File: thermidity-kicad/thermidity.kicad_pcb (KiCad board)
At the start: 2 copper layers, 60 x 30 mm, 17 parts, among them J1 Battery, J2 Display, J3 ISP, U1 ATmega328P, U2 HIH-5030, U3 TMP36

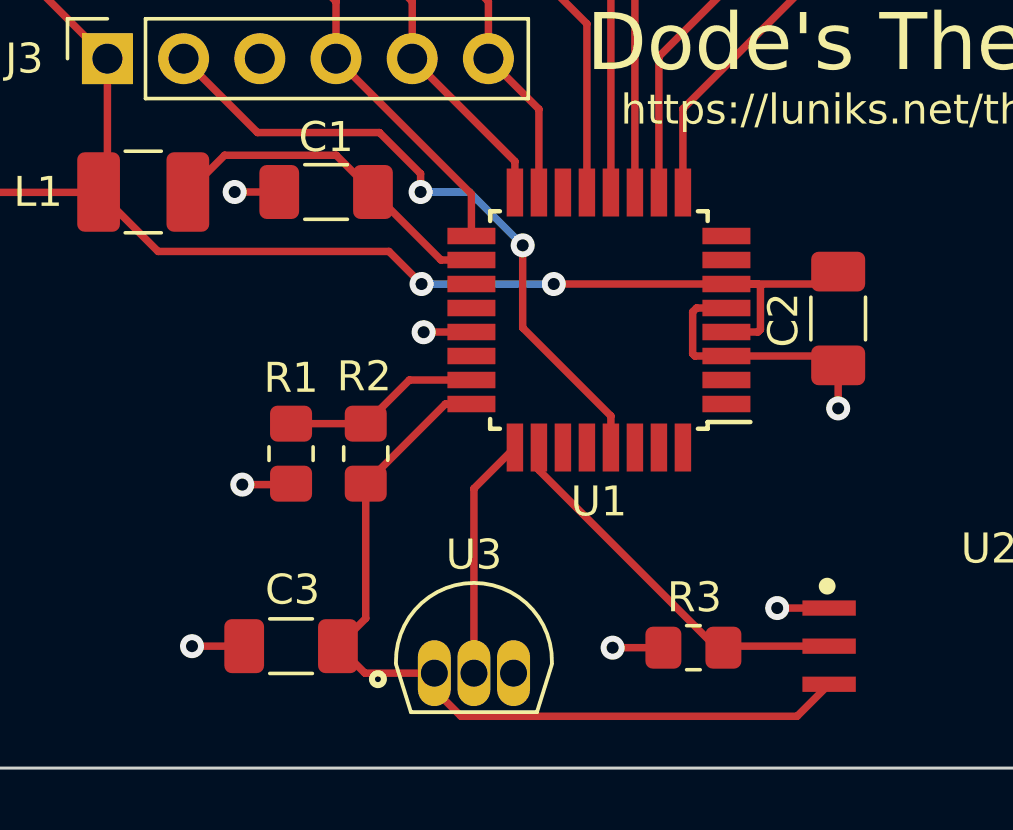
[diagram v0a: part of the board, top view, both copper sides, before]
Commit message: ratiometric measurement of temperature
- replace TMP36 with a thermistor NTC 100k
- put back 1nF cap between AREF and GND
- wait 150us for the cap to discharge before converting with 1.1V reference
- uint16_t is enough for 16x ADC
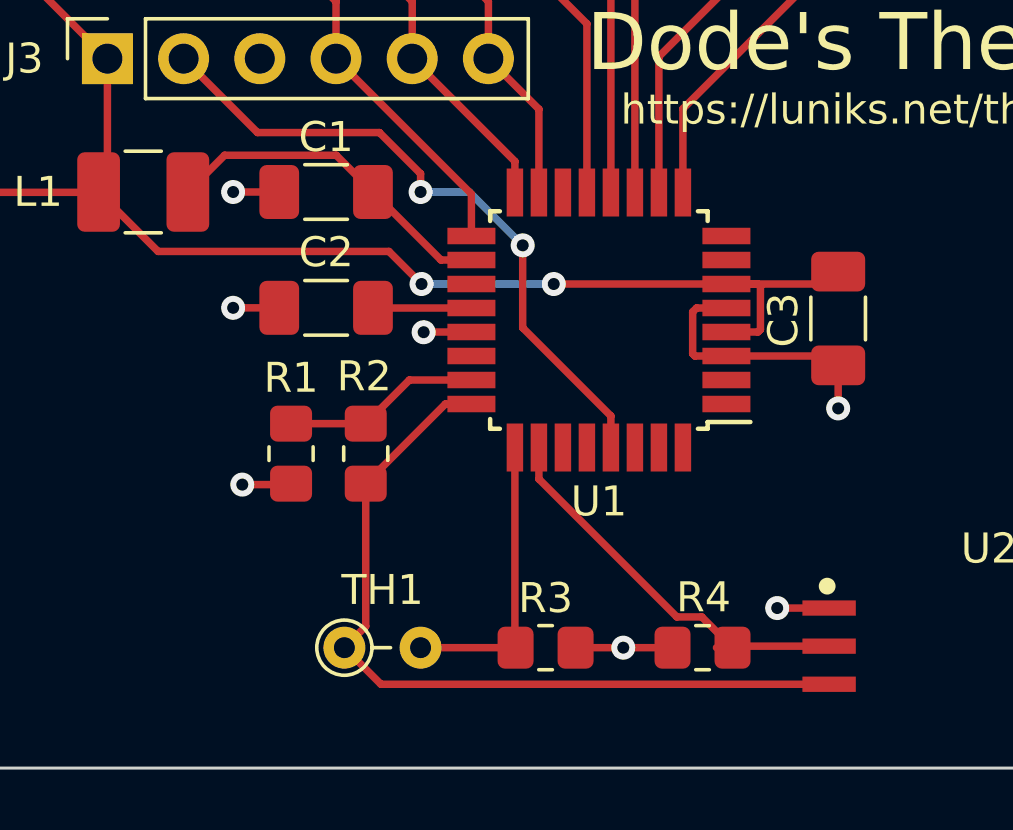
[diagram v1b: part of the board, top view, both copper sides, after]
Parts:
- removed the C3 at (135.2, 84.8)
- removed U3: TMP36, TMP36GT9:XDCR_TMP36GT9
- added C2: 1nF, Capacitor_SMD:C_1206_3216Metric_Pad1.33x1.80mm_HandSolder, F.Cu at (136.3, 73.6)
- added R3: 100k, Resistor_SMD:R_0805_2012Metric_Pad1.20x1.40mm_HandSolder, F.Cu at (143.7, 84.9)
- added TH1: NTC 100k, Resistor_THT:R_Axial_DIN0204_L3.6mm_D1.6mm_P2.54mm_Vertical, F.Cu at (137.0, 84.9)
- R1: value 1M -> 300K
- R2: value 1M -> 1.2M
- moved R4 0.30 mm to (148.9, 84.9)
- renumbered C2 to C3, R3 to R4
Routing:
- net unconnected-(U1-Pad20): track 0.00 -> 3.28 mm
- net Net-(U1-Pad25): track 8.09 -> 9.85 mm
- net Net-(R2-Pad1): track 28.5 -> 27.0 mm
- net GND: track 19.2 -> 20.5 mm
- net Net-(R4-Pad1): track 13.0 -> 13.7 mm

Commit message: ratiometric measurement of temperature
- SMD footprint instead of TH for thermistor
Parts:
- TH1: footprint Resistor_THT:R_Axial_DIN0204_L3.6mm_D1.6mm_P2.54mm_Vertical -> Resistor_SMD:R_1206_3216Metric_Pad1.30x1.75mm_HandSolder
- moved TH1 1.27 mm to (138.2, 84.9)
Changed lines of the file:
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@@
     )
   )
-  (footprint "Resistor_THT:R_Axial_DIN0204_L3.6mm_D1.6mm_P2.54mm_Vertical" (layer "F.Cu")
-    (at 136.956 84.8868)
-    (descr "Resistor, Axial_DIN0204 series, Axial, Vertical, pin pitch=2.54mm, 0.167W, length*diameter=3.6*1.6mm^2, http://cdn-reichelt.de/documents/datenblatt/B400/1_4W%23YAG.pdf")
-    (tags "Resistor Axial_DIN0204 series Axial Vertical pin pitch 2.54mm 0.167W length 3.6mm diameter 1.6mm")
-    (property "Sheetfile" "thermidity.kicad_sch")
-    (property "Sheetname" "")
-    (attr through_hole)
-    (fp_text reference "TH1" (at 1.27 -1.92) (layer "F.SilkS")
-      (effects (font (size 1 1) (thickness 0.15)))
-    )
-    (fp_text value "NTC 100k" (at 1.27 1.92) (layer "F.Fab")
-      (effects (font (size 1 1) (thickness 0.15)))
-    )
-    (fp_text user "${REFERENCE}" (at 1.27 -1.92) (layer "F.Fab")
-      (effects (font (size 1 1) (thickness 0.15)))
-    )
-    (fp_line (start 0.92 0) (end 1.54 0) (layer "F.SilkS") (width 0.12))
-    (fp_circle (center 0 0) (end 0.92 0) (layer "F.SilkS") (width 0.12) (fill none))
-    (fp_line (start 3.49 1.05) (end 3.49 -1.05) (layer "F.CrtYd") (width 0.05))
-    (fp_line (start 3.49 -1.05) (end -1.05 -1.05) (layer "F.CrtYd") (width 0.05))
-    (fp_line (start -1.05 1.05) (end 3.49 1.05) (layer "F.CrtYd") (width 0.05))
-    (fp_line (start -1.05 -1.05) (end -1.05 1.05) (layer "F.CrtYd") (width 0.05))
-    (fp_line (start 0 0) (end 2.54 0) (layer "F.Fab") (width 0.1))
-    (fp_circle (center 0 0) (end 0.8 0) (layer "F.Fab") (width 0.1) (fill none))
-    (pad "1" thru_hole circle (at 0 0) (size 1.4 1.4) (drill 0.7) (layers *.Cu *.Mask)
+  (footprint "Resistor_SMD:R_1206_3216Metric_Pad1.30x1.75mm_HandSolder" (layer "F.Cu")
+    (at 138.2268 84.8868)
+    (descr "Resistor SMD 1206 (3216 Metric), square (rectangular) end terminal, IPC_7351 nominal with elongated pad for handsoldering. (Body size source: IPC-SM-782 page 72, https://www.pcb-3d.com/wordpress/wp-content/uploads/ipc-sm-782a_amendment_1_and_2.pdf), generated with kicad-footprint-generator")
+    (tags "resistor handsolder")
+    (property "Sheetfile" "thermidity.kicad_sch")
+    (property "Sheetname" "")
+    (attr smd)
+    (fp_text reference "TH1" (at 0 -1.82) (layer "F.SilkS")
+      (effects (font (size 1 1) (thickness 0.15)))
+    )
+    (fp_text value "NTC 100k" (at 0 1.82) (layer "F.Fab")
+      (effects (font (size 1 1) (thickness 0.15)))
+    )
+    (fp_text user "${REFERENCE}" (at 0 0) (layer "F.Fab")
+      (effects (font (size 0.8 0.8) (thickness 0.12)))
+    )
+    (fp_line (start -0.727064 0.91) (end 0.727064 0.91) (layer "F.SilkS") (width 0.12))
+    (fp_line (start -0.727064 -0.91) (end 0.727064 -0.91) (layer "F.SilkS") (width 0.12))
+    (fp_line (start 2.45 1.12) (end -2.45 1.12) (layer "F.CrtYd") (width 0.05))
+    (fp_line (start -2.45 -1.12) (end 2.45 -1.12) (layer "F.CrtYd") (width 0.05))
+    (fp_line (start -2.45 1.12) (end -2.45 -1.12) (layer "F.CrtYd") (width 0.05))
+    (fp_line (start 2.45 -1.12) (end 2.45 1.12) (layer "F.CrtYd") (width 0.05))
+    (fp_line (start -1.6 0.8) (end -1.6 -0.8) (layer "F.Fab") (width 0.1))
+    (fp_line (start -1.6 -0.8) (end 1.6 -0.8) (layer "F.Fab") (width 0.1))
+    (fp_line (start 1.6 0.8) (end -1.6 0.8) (layer "F.Fab") (width 0.1))
+    (fp_line (start 1.6 -0.8) (end 1.6 0.8) (layer "F.Fab") (width 0.1))
+    (pad "1" smd roundrect (at -1.55 0) (size 1.3 1.75) (layers "F.Cu" "F.Paste" "F.Mask") (roundrect_rratio 0.192308)
       (net 15 "Net-(R2-Pad1)") (pintype "passive"))
-    (pad "2" thru_hole oval (at 2.54 0) (size 1.4 1.4) (drill 0.7) (layers *.Cu *.Mask)
+    (pad "2" smd roundrect (at 1.55 0) (size 1.3 1.75) (layers "F.Cu" "F.Paste" "F.Mask") (roundrect_rratio 0.192308)
       (net 24 "Net-(U1-Pad25)") (pintype "passive"))
-    (model "${KICAD6_3DMODEL_DIR}/Resistor_THT.3dshapes/R_Axial_DIN0204_L3.6mm_D1.6mm_P2.54mm_Vertical.wrl"
+    (model "${KICAD6_3DMODEL_DIR}/Resistor_SMD.3dshapes/R_1206_3216Metric.wrl"
       (offset (xyz 0 0 0))
       (scale (xyz 1 1 1))
@@
   (segment (start 141.1224 69.6976) (end 142.9004 71.4756) (width 0.25) (layer "B.Cu") (net 14))
   (segment (start 139.4968 69.6976) (end 141.1224 69.6976) (width 0.25) (layer "B.Cu") (net 14))
-  (segment (start 138.1752 86.106) (end 153.1142 86.106) (width 0.25) (layer "F.Cu") (net 15))
   (segment (start 140.3224 76.7648) (end 137.668 79.4192) (width 0.25) (layer "F.Cu") (net 15))
-  (segment (start 137.668 84.1748) (end 136.956 84.8868) (width 0.25) (layer "F.Cu") (net 15))
-  (segment (start 137.668 79.4192) (end 137.668 84.1748) (width 0.25) (layer "F.Cu") (net 15))
-  (segment (start 136.956 84.8868) (end 138.1752 86.106) (width 0.25) (layer "F.Cu") (net 15))
+  (segment (start 136.6768 84.8868) (end 137.896 86.106) (width 0.25) (layer "F.Cu") (net 15))
+  (segment (start 137.896 86.106) (end 153.1142 86.106) (width 0.25) (layer "F.Cu") (net 15))
+  (segment (start 137.668 83.8956) (end 136.6768 84.8868) (width 0.25) (layer "F.Cu") (net 15))
+  (segment (start 137.668 79.4192) (end 137.668 83.8956) (width 0.25) (layer "F.Cu") (net 15))
   (segment (start 141.1904 76.7648) (end 140.3224 76.7648) (width 0.25) (layer "F.Cu") (net 15))
   (segment (start 137.9161 73.5648) (end 137.9097 73.5584) (width 0.25) (layer "F.Cu") (net 16))
   (segment (start 141.1904 73.5648) (end 137.9161 73.5648) (width 0.25) (layer "F.Cu") (net 16))
-  (segment (start 139.496 84.8868) (end 142.6624 84.8868) (width 0.25) (layer "F.Cu") (net 24))
+  (segment (start 142.6624 84.8868) (end 139.7768 84.8868) (width 0.25) (layer "F.Cu") (net 24))
   (segment (start 142.6404 78.2148) (end 142.6404 84.8648) (width 0.25) (layer "F.Cu") (net 24))
   (segment (start 142.6404 84.8648) (end 142.6624 84.8868) (width 0.25) (layer "F.Cu") (net 24))

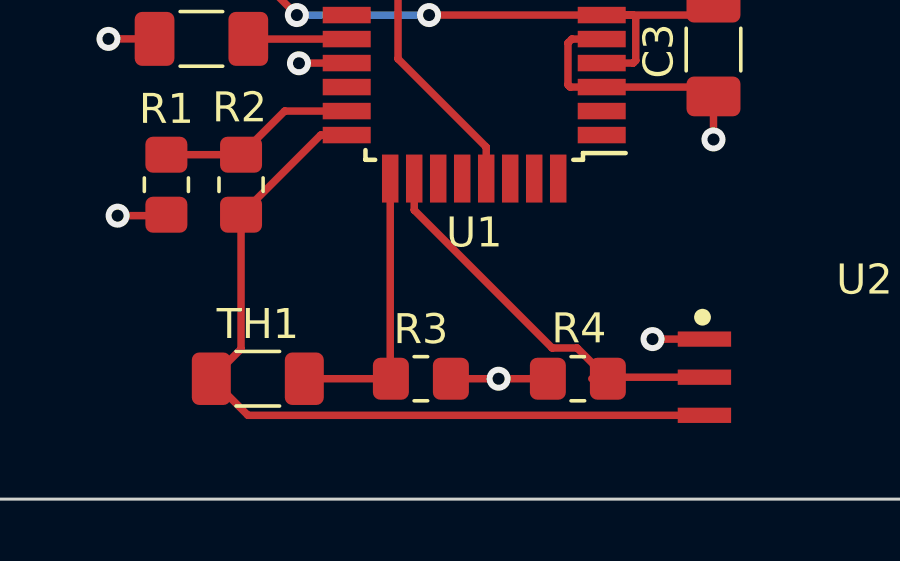
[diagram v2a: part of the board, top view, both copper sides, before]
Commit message: ratiometric measurement of temperature
- calculate temperature
- rounding of temperature compensated relative humidity
- no need for battery voltage in mV
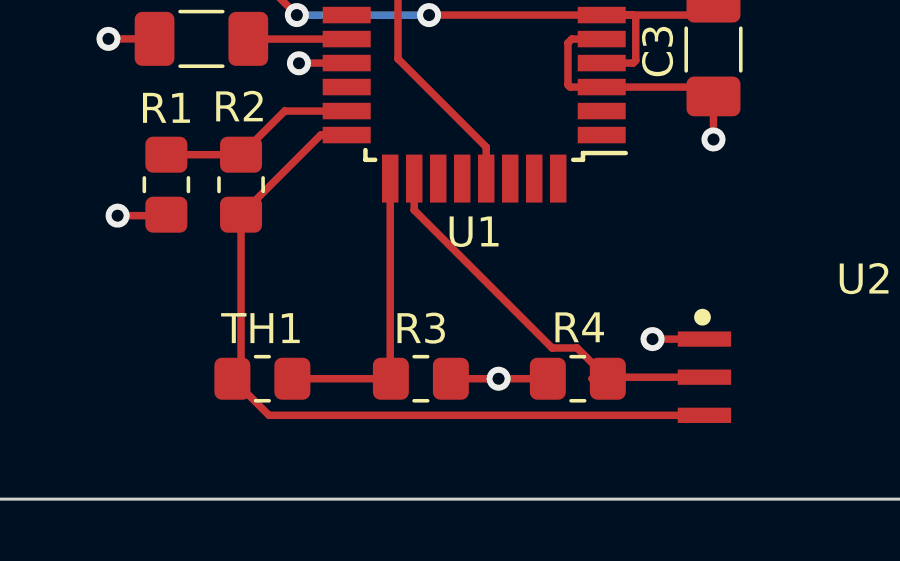
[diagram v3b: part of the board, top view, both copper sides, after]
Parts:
- TH1: footprint Resistor_SMD:R_1206_3216Metric_Pad1.30x1.75mm_HandSolder -> Resistor_SMD:R_0805_2012Metric_Pad1.20x1.40mm_HandSolder
- moved TH1 0.15 mm to (138.4, 84.9)
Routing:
- net Net-(R2-Pad1): track 27.4 -> 26.4 mm
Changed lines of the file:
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@@
     )
   )
-  (footprint "Resistor_SMD:R_1206_3216Metric_Pad1.30x1.75mm_HandSolder" (layer "F.Cu")
-    (at 138.2268 84.8868)
-    (descr "Resistor SMD 1206 (3216 Metric), square (rectangular) end terminal, IPC_7351 nominal with elongated pad for handsoldering. (Body size source: IPC-SM-782 page 72, https://www.pcb-3d.com/wordpress/wp-content/uploads/ipc-sm-782a_amendment_1_and_2.pdf), generated with kicad-footprint-generator")
+  (footprint "Resistor_SMD:R_0805_2012Metric_Pad1.20x1.40mm_HandSolder" (layer "F.Cu")
+    (at 138.3792 84.8868)
+    (descr "Resistor SMD 0805 (2012 Metric), square (rectangular) end terminal, IPC_7351 nominal with elongated pad for handsoldering. (Body size source: IPC-SM-782 page 72, https://www.pcb-3d.com/wordpress/wp-content/uploads/ipc-sm-782a_amendment_1_and_2.pdf), generated with kicad-footprint-generator")
     (tags "resistor handsolder")
     (property "Sheetfile" "thermidity.kicad_sch")
     (property "Sheetname" "")
     (attr smd)
-    (fp_text reference "TH1" (at 0 -1.82) (layer "F.SilkS")
-      (effects (font (size 1 1) (thickness 0.15)))
-    )
-    (fp_text value "NTC 100k" (at 0 1.82) (layer "F.Fab")
-      (effects (font (size 1 1) (thickness 0.15)))
-    )
-    (fp_text user "${REFERENCE}" (at 0 0) (layer "F.Fab")
-      (effects (font (size 0.8 0.8) (thickness 0.12)))
-    )
-    (fp_line (start -0.727064 0.91) (end 0.727064 0.91) (layer "F.SilkS") (width 0.12))
-    (fp_line (start -0.727064 -0.91) (end 0.727064 -0.91) (layer "F.SilkS") (width 0.12))
-    (fp_line (start 2.45 1.12) (end -2.45 1.12) (layer "F.CrtYd") (width 0.05))
-    (fp_line (start -2.45 -1.12) (end 2.45 -1.12) (layer "F.CrtYd") (width 0.05))
-    (fp_line (start -2.45 1.12) (end -2.45 -1.12) (layer "F.CrtYd") (width 0.05))
-    (fp_line (start 2.45 -1.12) (end 2.45 1.12) (layer "F.CrtYd") (width 0.05))
-    (fp_line (start -1.6 0.8) (end -1.6 -0.8) (layer "F.Fab") (width 0.1))
-    (fp_line (start -1.6 -0.8) (end 1.6 -0.8) (layer "F.Fab") (width 0.1))
-    (fp_line (start 1.6 0.8) (end -1.6 0.8) (layer "F.Fab") (width 0.1))
-    (fp_line (start 1.6 -0.8) (end 1.6 0.8) (layer "F.Fab") (width 0.1))
-    (pad "1" smd roundrect (at -1.55 0) (size 1.3 1.75) (layers "F.Cu" "F.Paste" "F.Mask") (roundrect_rratio 0.192308)
+    (fp_text reference "TH1" (at 0 -1.65) (layer "F.SilkS")
+      (effects (font (size 1 1) (thickness 0.15)))
+    )
+    (fp_text value "NTC 100k" (at 0 1.65) (layer "F.Fab")
+      (effects (font (size 1 1) (thickness 0.15)))
+    )
+    (fp_text user "${REFERENCE}" (at 0 0) (layer "F.Fab")
+      (effects (font (size 0.5 0.5) (thickness 0.08)))
+    )
+    (fp_line (start -0.227064 -0.735) (end 0.227064 -0.735) (layer "F.SilkS") (width 0.12))
+    (fp_line (start -0.227064 0.735) (end 0.227064 0.735) (layer "F.SilkS") (width 0.12))
+    (fp_line (start -1.85 0.95) (end -1.85 -0.95) (layer "F.CrtYd") (width 0.05))
+    (fp_line (start 1.85 -0.95) (end 1.85 0.95) (layer "F.CrtYd") (width 0.05))
+    (fp_line (start -1.85 -0.95) (end 1.85 -0.95) (layer "F.CrtYd") (width 0.05))
+    (fp_line (start 1.85 0.95) (end -1.85 0.95) (layer "F.CrtYd") (width 0.05))
+    (fp_line (start -1 -0.625) (end 1 -0.625) (layer "F.Fab") (width 0.1))
+    (fp_line (start 1 0.625) (end -1 0.625) (layer "F.Fab") (width 0.1))
+    (fp_line (start 1 -0.625) (end 1 0.625) (layer "F.Fab") (width 0.1))
+    (fp_line (start -1 0.625) (end -1 -0.625) (layer "F.Fab") (width 0.1))
+    (pad "1" smd roundrect (at -1 0) (size 1.2 1.4) (layers "F.Cu" "F.Paste" "F.Mask") (roundrect_rratio 0.208333)
       (net 15 "Net-(R2-Pad1)") (pintype "passive"))
-    (pad "2" smd roundrect (at 1.55 0) (size 1.3 1.75) (layers "F.Cu" "F.Paste" "F.Mask") (roundrect_rratio 0.192308)
+    (pad "2" smd roundrect (at 1 0) (size 1.2 1.4) (layers "F.Cu" "F.Paste" "F.Mask") (roundrect_rratio 0.208333)
       (net 24 "Net-(U1-Pad25)") (pintype "passive"))
-    (model "${KICAD6_3DMODEL_DIR}/Resistor_SMD.3dshapes/R_1206_3216Metric.wrl"
+    (model "${KICAD6_3DMODEL_DIR}/Resistor_SMD.3dshapes/R_0805_2012Metric.wrl"
       (offset (xyz 0 0 0))
       (scale (xyz 1 1 1))
@@
   (segment (start 139.4968 69.6976) (end 141.1224 69.6976) (width 0.25) (layer "B.Cu") (net 14))
   (segment (start 140.3224 76.7648) (end 137.668 79.4192) (width 0.25) (layer "F.Cu") (net 15))
-  (segment (start 136.6768 84.8868) (end 137.896 86.106) (width 0.25) (layer "F.Cu") (net 15))
-  (segment (start 137.896 86.106) (end 153.1142 86.106) (width 0.25) (layer "F.Cu") (net 15))
-  (segment (start 137.668 83.8956) (end 136.6768 84.8868) (width 0.25) (layer "F.Cu") (net 15))
-  (segment (start 137.668 79.4192) (end 137.668 83.8956) (width 0.25) (layer "F.Cu") (net 15))
+  (segment (start 137.668 84.598) (end 137.3792 84.8868) (width 0.25) (layer "F.Cu") (net 15))
+  (segment (start 137.668 79.4192) (end 137.668 84.598) (width 0.25) (layer "F.Cu") (net 15))
+  (segment (start 138.5984 86.106) (end 153.1142 86.106) (width 0.25) (layer "F.Cu") (net 15))
+  (segment (start 137.3792 84.8868) (end 138.5984 86.106) (width 0.25) (layer "F.Cu") (net 15))
   (segment (start 141.1904 76.7648) (end 140.3224 76.7648) (width 0.25) (layer "F.Cu") (net 15))
   (segment (start 137.9161 73.5648) (end 137.9097 73.5584) (width 0.25) (layer "F.Cu") (net 16))
   (segment (start 141.1904 73.5648) (end 137.9161 73.5648) (width 0.25) (layer "F.Cu") (net 16))
-  (segment (start 142.6624 84.8868) (end 139.7768 84.8868) (width 0.25) (layer "F.Cu") (net 24))
   (segment (start 142.6404 78.2148) (end 142.6404 84.8648) (width 0.25) (layer "F.Cu") (net 24))
   (segment (start 142.6404 84.8648) (end 142.6624 84.8868) (width 0.25) (layer "F.Cu") (net 24))
+  (segment (start 139.3792 84.8868) (end 142.6624 84.8868) (width 0.25) (layer "F.Cu") (net 24))
   (segment (start 136.6847 68.4726) (end 132.9637 68.4726) (width 0.25) (layer "F.Cu") (net 31))
   (segment (start 132.9637 68.4726) (end 131.7387 69.6976) (width 0.25) (layer "F.Cu") (net 31))
